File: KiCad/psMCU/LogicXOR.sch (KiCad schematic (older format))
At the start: 18 parts

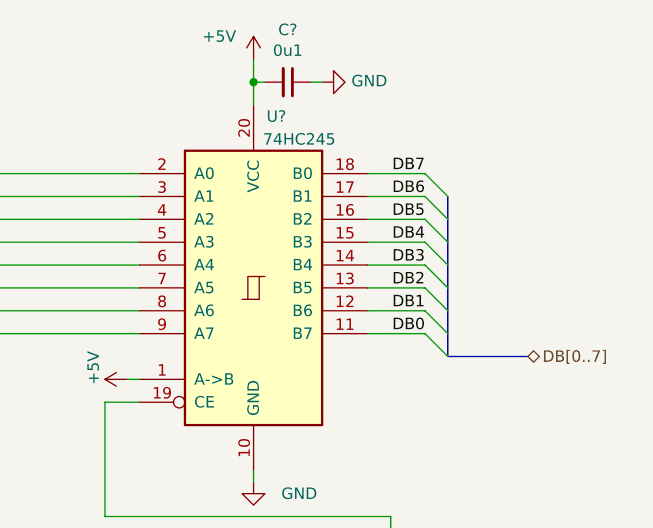
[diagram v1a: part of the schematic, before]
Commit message: First ERC pass
    All unconnects solved, need to inspect Tristate errors.
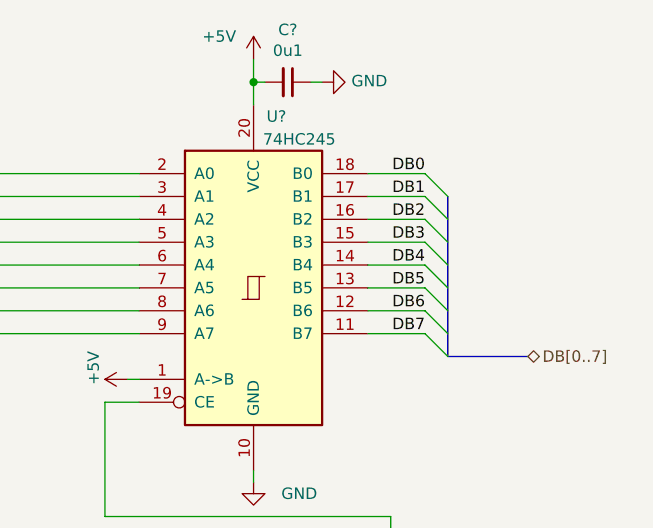
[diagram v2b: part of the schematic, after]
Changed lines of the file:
@@
 $Descr A4 11693 8268
 encoding utf-8
-Sheet 103 209
+Sheet 68 207
 Title "psMCU"
 Date ""
@@
 Entry Wire Line
 	6900 1950 7000 2050
+Text Label 6900 1250 2    50   ~ 0
+DB0
+Text Label 6900 1350 2    50   ~ 0
+DB1
+Text Label 6900 1450 2    50   ~ 0
+DB2
+Text Label 6900 1550 2    50   ~ 0
+DB3
+Text Label 6900 1650 2    50   ~ 0
+DB4
+Text Label 6900 1750 2    50   ~ 0
+DB5
+Text Label 6900 1850 2    50   ~ 0
+DB6
 Text Label 6900 1950 2    50   ~ 0
-DB0
-Text Label 6900 1850 2    50   ~ 0
-DB1
-Text Label 6900 1750 2    50   ~ 0
-DB2
-Text Label 6900 1650 2    50   ~ 0
-DB3
-Text Label 6900 1550 2    50   ~ 0
-DB4
-Text Label 6900 1450 2    50   ~ 0
-DB5
-Text Label 6900 1350 2    50   ~ 0
-DB6
-Text Label 6900 1250 2    50   ~ 0
 DB7
+Wire Wire Line
+	6650 1950 6900 1950
+Wire Wire Line
+	6650 1850 6900 1850
+Wire Wire Line
+	6650 1750 6900 1750
+Wire Wire Line
+	6650 1650 6900 1650
+Wire Wire Line
+	6650 1550 6900 1550
+Wire Wire Line
+	6650 1450 6900 1450
+Wire Wire Line
+	6650 1350 6900 1350
 Wire Wire Line
 	6650 1250 6900 1250
 Wire Wire Line
-	6650 1350 6900 1350
-Wire Wire Line
-	6650 1450 6900 1450
-Wire Wire Line
-	6650 1550 6900 1550
-Wire Wire Line
-	6650 1650 6900 1650
-Wire Wire Line
-	6650 1750 6900 1750
-Wire Wire Line
-	6650 1850 6900 1850
-Wire Wire Line
-	6650 1950 6900 1950
-Wire Wire Line
 	4350 1250 5650 1250

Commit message: First Schematic Draft done.
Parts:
- C134, C135, C136, C137, C138: renamed from C?; footprint Capacitor_SMD:C_0603_1608Metric -> NoRef_Footprints:C_0603_1608Metric_NoRef
- gave numbers to parts that had none: 5

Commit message: Small improvements.
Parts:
- renumbered C134 to C132, C135 to C133, C136 to C134, C137 to C135, C138 to C136, U134 to U132, U135 to U133, U136 to U134, U137 to U135, U138 to U136

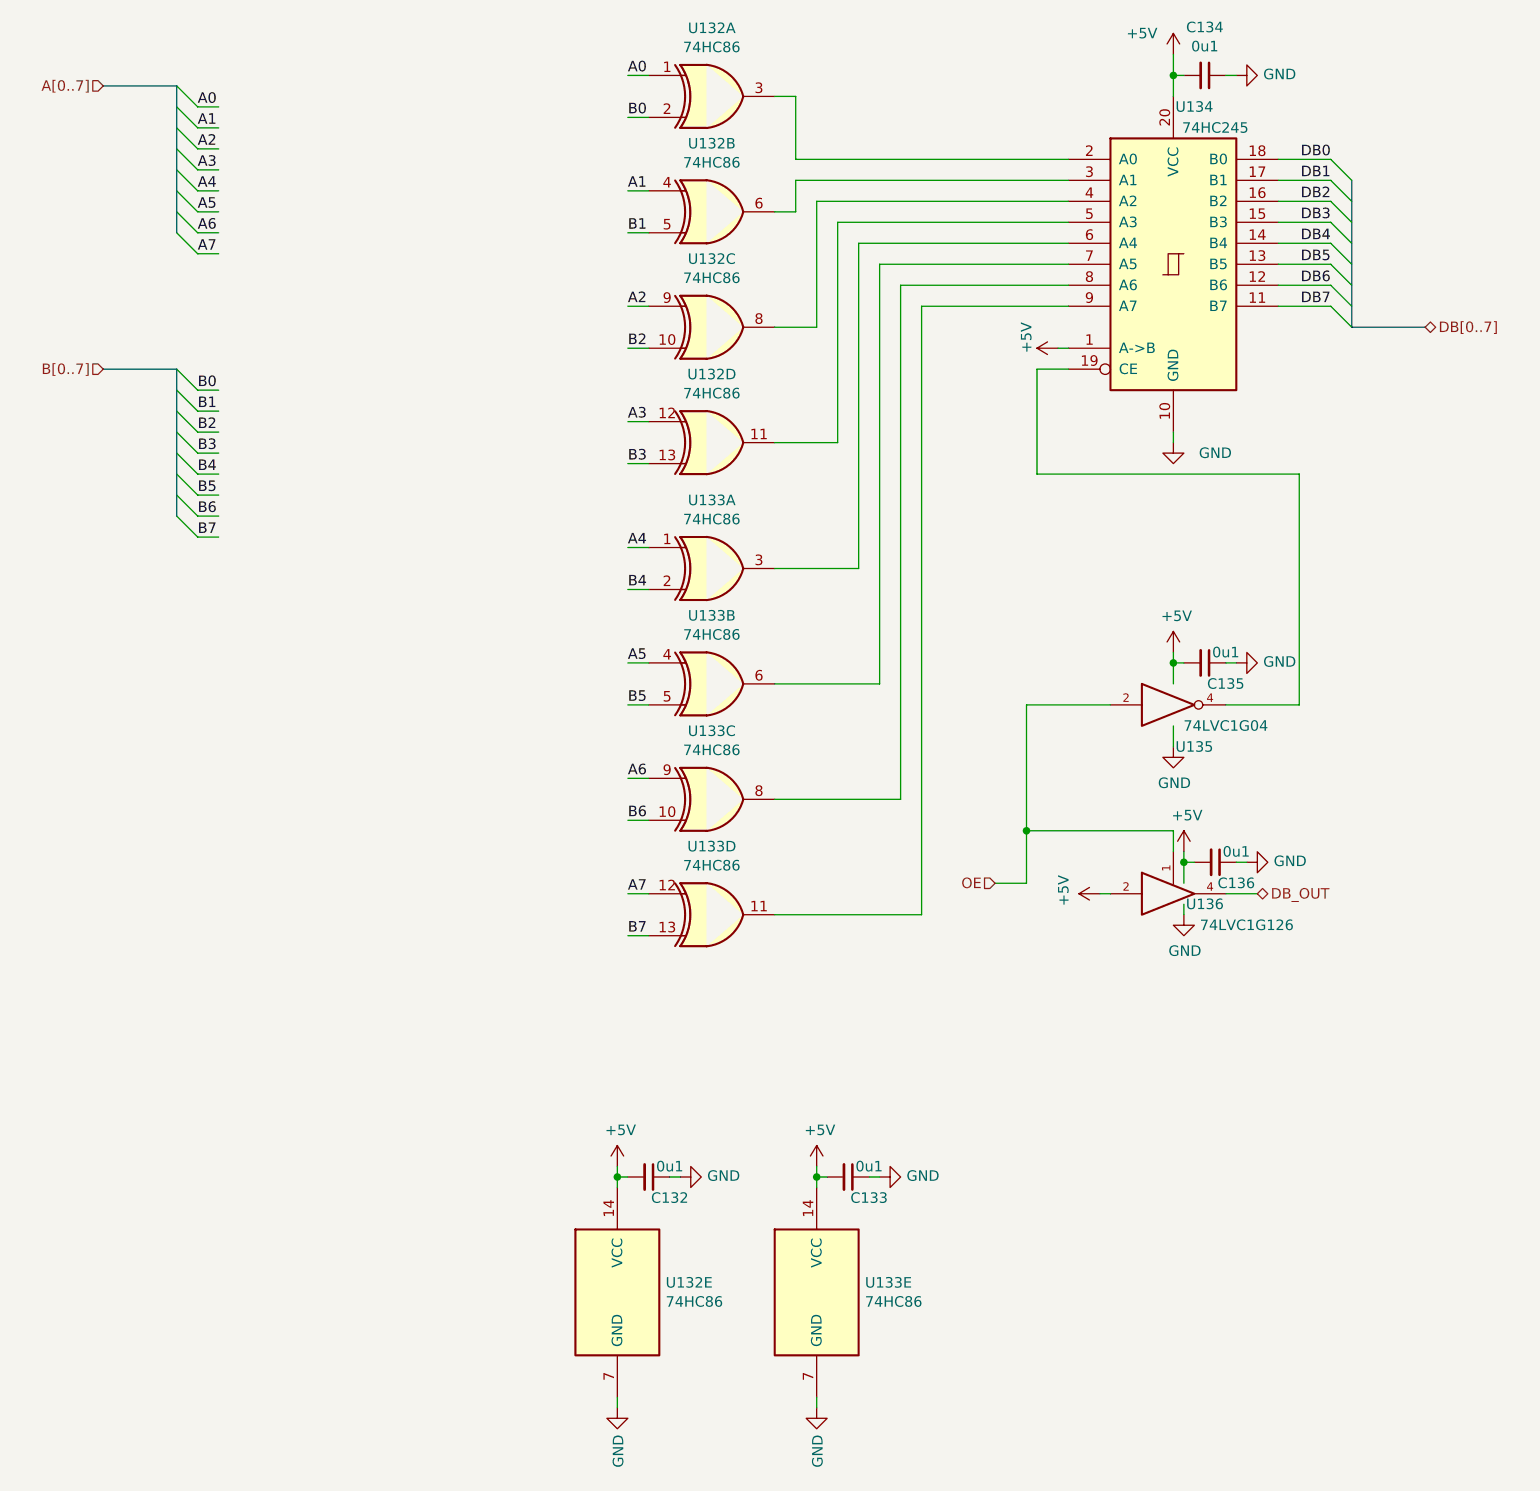
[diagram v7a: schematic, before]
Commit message: Updated values and footprints.
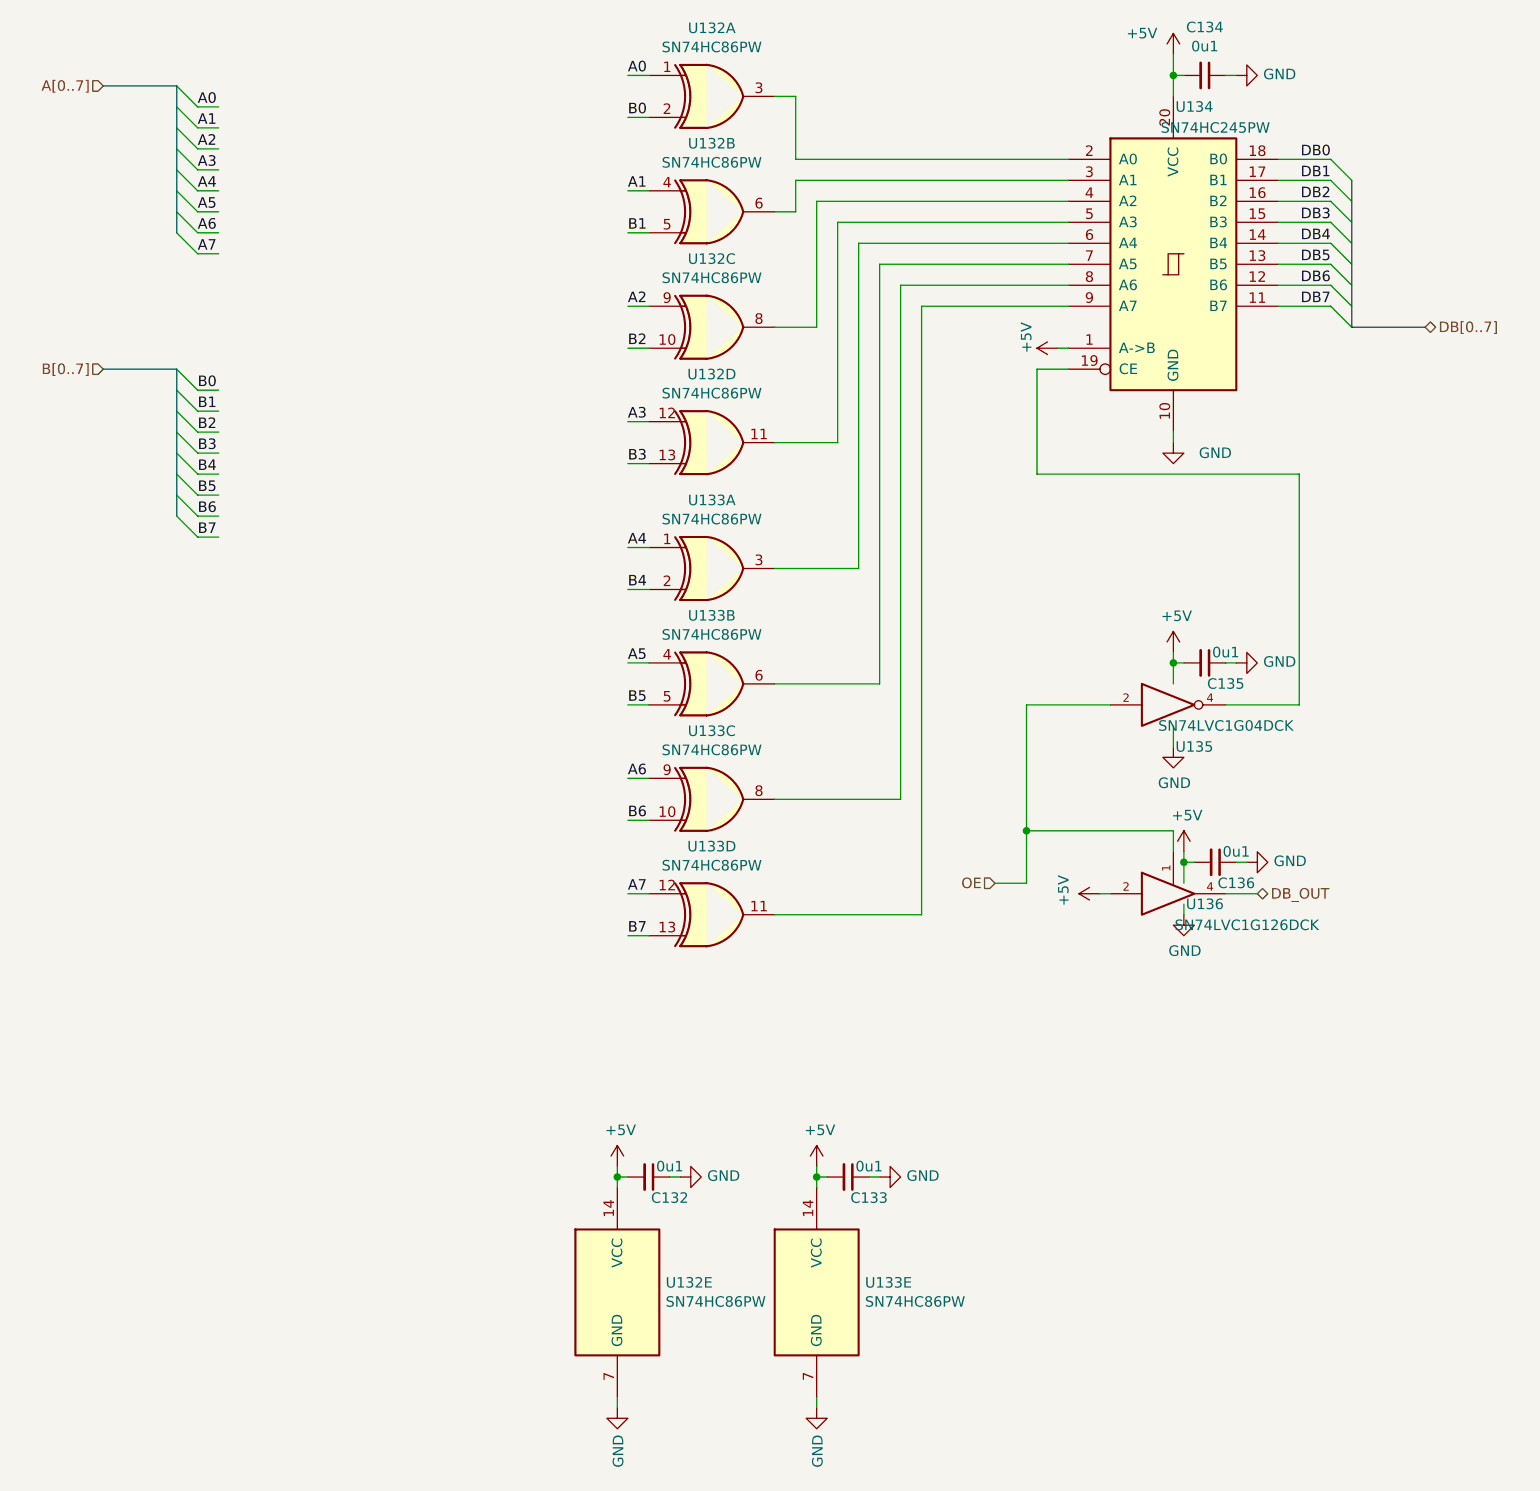
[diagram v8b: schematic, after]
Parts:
- U132, U133: value 74HC86 -> SN74HC86PW; footprint (none) -> Package_SO:TSSOP-14_4.4x5mm_P0.65mm
- U134: value 74HC245 -> SN74HC245PW; footprint Package_SO:SSOP-20_5.3x7.2mm_P0.65mm -> Package_SO:TSSOP-20_4.4x6.5mm_P0.65mm
- U135: value 74LVC1G04 -> SN74LVC1G04DCK
- U136: value 74LVC1G126 -> SN74LVC1G126DCK
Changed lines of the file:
@@
 AR Path="/5FF66C9F/600C3422/60543CB5" Ref="U134"  Part="1"
 F 0 "U134" H 6250 2500 50  0000 C CNN
-F 1 "74HC245" H 6350 2400 50  0000 C CNN
-F 2 "Package_SO:SSOP-20_5.3x7.2mm_P0.65mm" H 6150 1750 50  0001 C CNN
+F 1 "SN74HC245PW" H 6350 2400 50  0000 C CNN
+F 2 "Package_SO:TSSOP-20_4.4x6.5mm_P0.65mm" H 6150 1750 50  0001 C CNN
 F 3 "http://www.ti.com/lit/gpn/sn74HC245" H 6150 1750 50  0001 C CNN
 	1    6150 1750
@@
 AR Path="/5FF66C9F/600C3422/60419346" Ref="U135"  Part="1"
 F 0 "U135" H 6250 3650 50  0000 C CNN
-F 1 "74LVC1G04" H 6400 3750 50  0000 C CNN
+F 1 "SN74LVC1G04DCK" H 6400 3750 50  0000 C CNN
 F 2 "Package_TO_SOT_SMD:SOT-353_SC-70-5" H 6150 3850 50  0001 C CNN
 F 3 "http://www.ti.com/lit/sg/scyt129e/scyt129e.pdf" H 6150 3850 50  0001 C CNN
@@
 AR Path="/5FF66C9F/600C3422/60142E92" Ref="U136"  Part="1"
 F 0 "U136" H 6300 4700 50  0000 C CNN
-F 1 "74LVC1G126" H 6500 4600 50  0000 C CNN
+F 1 "SN74LVC1G126DCK" H 6500 4600 50  0000 C CNN
 F 2 "Package_TO_SOT_SMD:SOT-353_SC-70-5" H 6150 4750 50  0001 C CNN
 F 3 "http://www.ti.com/lit/sg/scyt129e/scyt129e.pdf" H 6150 4750 50  0001 C CNN
@@
 AR Path="/5FF66C9F/600C3422/6061A13D" Ref="U132"  Part="1"
 F 0 "U132" H 3950 1275 50  0000 C CNN
-F 1 "74HC86" H 3950 1184 50  0000 C CNN
-F 2 "" H 3950 950 50  0001 C CNN
+F 1 "SN74HC86PW" H 3950 1184 50  0000 C CNN
+F 2 "Package_SO:TSSOP-14_4.4x5mm_P0.65mm" H 3950 950 50  0001 C CNN
 F 3 "http://www.ti.com/lit/gpn/sn74HC86" H 3950 950 50  0001 C CNN
 	1    3950 950
@@
 AR Path="/5FF66C9F/600C3422/6061A143" Ref="U132"  Part="2"
 F 0 "U132" H 3950 1825 50  0000 C CNN
-F 1 "74HC86" H 3950 1734 50  0000 C CNN
-F 2 "" H 3950 1500 50  0001 C CNN
+F 1 "SN74HC86PW" H 3950 1734 50  0000 C CNN
+F 2 "Package_SO:TSSOP-14_4.4x5mm_P0.65mm" H 3950 1500 50  0001 C CNN
 F 3 "http://www.ti.com/lit/gpn/sn74HC86" H 3950 1500 50  0001 C CNN
 	2    3950 1500
@@
 AR Path="/5FF66C9F/600C3422/6061A149" Ref="U132"  Part="3"
 F 0 "U132" H 3950 2375 50  0000 C CNN
-F 1 "74HC86" H 3950 2284 50  0000 C CNN
-F 2 "" H 3950 2050 50  0001 C CNN
+F 1 "SN74HC86PW" H 3950 2284 50  0000 C CNN
+F 2 "Package_SO:TSSOP-14_4.4x5mm_P0.65mm" H 3950 2050 50  0001 C CNN
 F 3 "http://www.ti.com/lit/gpn/sn74HC86" H 3950 2050 50  0001 C CNN
 	3    3950 2050
@@
 AR Path="/5FF66C9F/600C3422/6061A14F" Ref="U132"  Part="4"
 F 0 "U132" H 3950 2925 50  0000 C CNN
-F 1 "74HC86" H 3950 2834 50  0000 C CNN
-F 2 "" H 3950 2600 50  0001 C CNN
+F 1 "SN74HC86PW" H 3950 2834 50  0000 C CNN
+F 2 "Package_SO:TSSOP-14_4.4x5mm_P0.65mm" H 3950 2600 50  0001 C CNN
 F 3 "http://www.ti.com/lit/gpn/sn74HC86" H 3950 2600 50  0001 C CNN
 	4    3950 2600
@@
 AR Path="/5FF66C9F/600C3422/6061A155" Ref="U132"  Part="5"
 F 0 "U132" H 3730 6696 50  0000 L CNN
-F 1 "74HC86" H 3730 6605 50  0000 L CNN
-F 2 "" H 3500 6650 50  0001 C CNN
+F 1 "SN74HC86PW" H 3730 6605 50  0000 L CNN
+F 2 "Package_SO:TSSOP-14_4.4x5mm_P0.65mm" H 3500 6650 50  0001 C CNN
 F 3 "http://www.ti.com/lit/gpn/sn74HC86" H 3500 6650 50  0001 C CNN
 	5    3500 6650
@@
 AR Path="/5FF66C9F/600C3422/6062E795" Ref="U133"  Part="1"
 F 0 "U133" H 3950 3525 50  0000 C CNN
-F 1 "74HC86" H 3950 3434 50  0000 C CNN
-F 2 "" H 3950 3200 50  0001 C CNN
+F 1 "SN74HC86PW" H 3950 3434 50  0000 C CNN
+F 2 "Package_SO:TSSOP-14_4.4x5mm_P0.65mm" H 3950 3200 50  0001 C CNN
 F 3 "http://www.ti.com/lit/gpn/sn74HC86" H 3950 3200 50  0001 C CNN
 	1    3950 3200
@@
 AR Path="/5FF66C9F/600C3422/6062E79B" Ref="U133"  Part="2"
 F 0 "U133" H 3950 4075 50  0000 C CNN
-F 1 "74HC86" H 3950 3984 50  0000 C CNN
-F 2 "" H 3950 3750 50  0001 C CNN
+F 1 "SN74HC86PW" H 3950 3984 50  0000 C CNN
+F 2 "Package_SO:TSSOP-14_4.4x5mm_P0.65mm" H 3950 3750 50  0001 C CNN
 F 3 "http://www.ti.com/lit/gpn/sn74HC86" H 3950 3750 50  0001 C CNN
 	2    3950 3750
@@
 AR Path="/5FF66C9F/600C3422/6062E7A1" Ref="U133"  Part="3"
 F 0 "U133" H 3950 4625 50  0000 C CNN
-F 1 "74HC86" H 3950 4534 50  0000 C CNN
-F 2 "" H 3950 4300 50  0001 C CNN
+F 1 "SN74HC86PW" H 3950 4534 50  0000 C CNN
+F 2 "Package_SO:TSSOP-14_4.4x5mm_P0.65mm" H 3950 4300 50  0001 C CNN
 F 3 "http://www.ti.com/lit/gpn/sn74HC86" H 3950 4300 50  0001 C CNN
 	3    3950 4300
@@
 AR Path="/5FF66C9F/600C3422/6062E7A7" Ref="U133"  Part="4"
 F 0 "U133" H 3950 5175 50  0000 C CNN
-F 1 "74HC86" H 3950 5084 50  0000 C CNN
-F 2 "" H 3950 4850 50  0001 C CNN
+F 1 "SN74HC86PW" H 3950 5084 50  0000 C CNN
+F 2 "Package_SO:TSSOP-14_4.4x5mm_P0.65mm" H 3950 4850 50  0001 C CNN
 F 3 "http://www.ti.com/lit/gpn/sn74HC86" H 3950 4850 50  0001 C CNN
 	4    3950 4850
@@
 AR Path="/5FF66C9F/600C3422/6062E7AD" Ref="U133"  Part="5"
 F 0 "U133" H 4680 6696 50  0000 L CNN
-F 1 "74HC86" H 4680 6605 50  0000 L CNN
-F 2 "" H 4450 6650 50  0001 C CNN
+F 1 "SN74HC86PW" H 4680 6605 50  0000 L CNN
+F 2 "Package_SO:TSSOP-14_4.4x5mm_P0.65mm" H 4450 6650 50  0001 C CNN
 F 3 "http://www.ti.com/lit/gpn/sn74HC86" H 4450 6650 50  0001 C CNN
 	5    4450 6650
